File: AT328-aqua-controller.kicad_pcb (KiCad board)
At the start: 2 copper layers, 76.6 x 76 mm, 46 parts, among them Q1 IRL520N, Q2 IRL520N, Q3 IRL520N, Q4 IRL520N, Q5 BC547, U1 ATmega328P-PU, U2 LM7805_TO220, Y1 16MHz

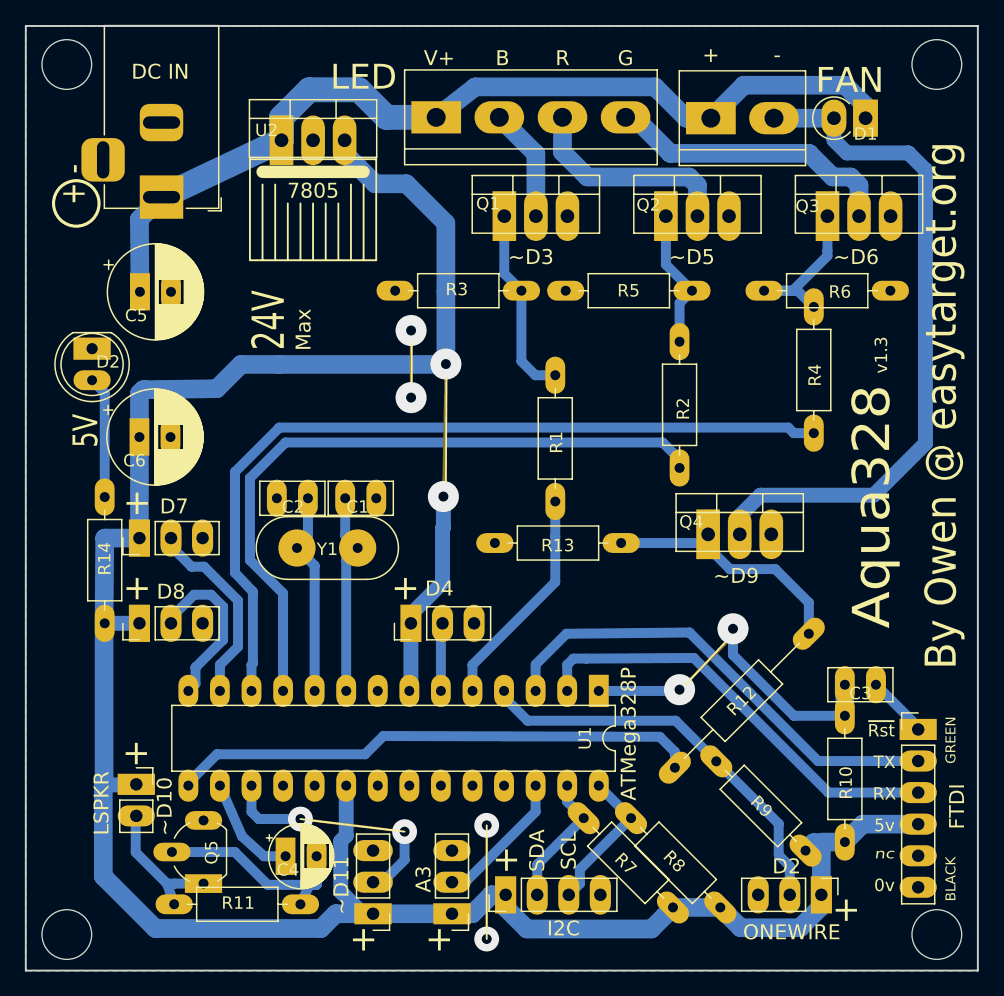
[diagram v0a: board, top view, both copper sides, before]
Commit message: New speaker circuit, updated PCB to suit and slight case mods.
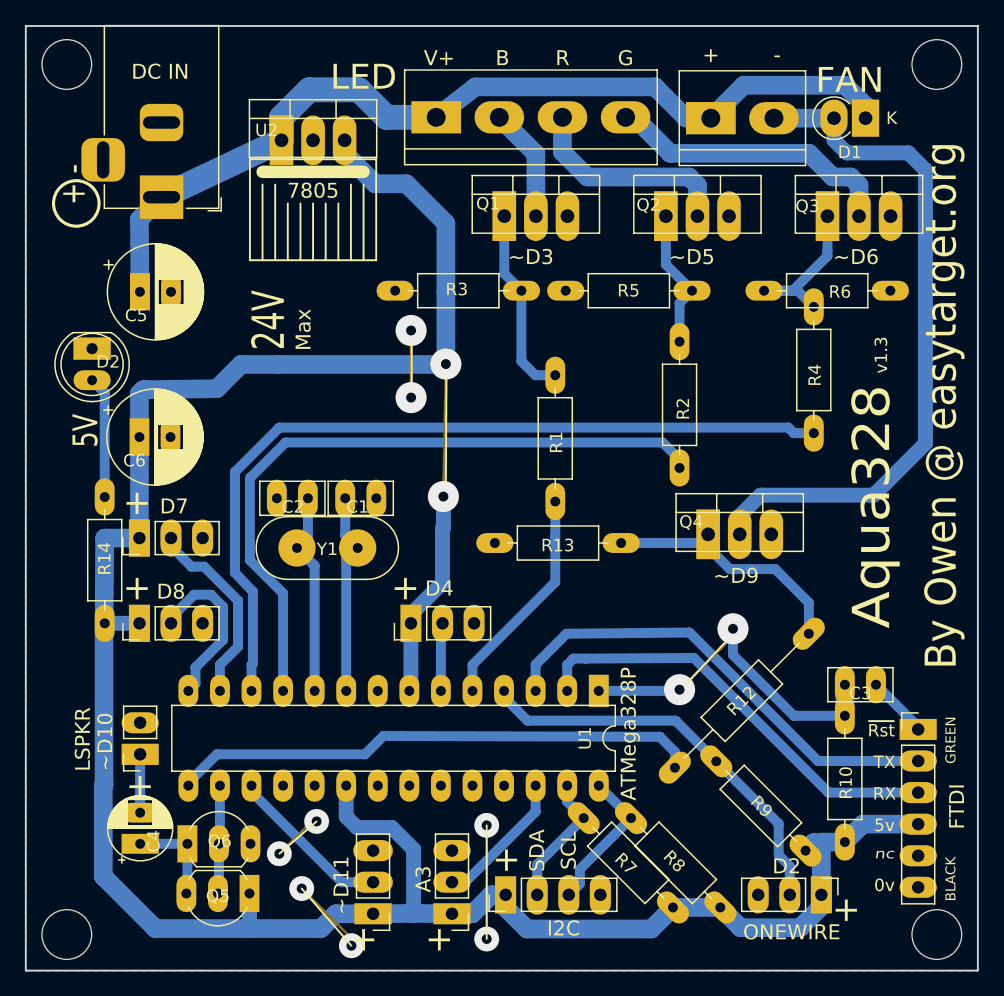
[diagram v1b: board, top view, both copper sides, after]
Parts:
- removed R11: 2K2, Resistor_THT:R_Axial_DIN0207_L6.3mm_D2.5mm_P10.16mm_Horizontal
- added Q6: BC327, Package_TO_SOT_THT:TO-92_Inline_Wide, F.Cu at (44.8, 93.3)
- C4: value 47uF -> 470uF
- Q5: value BC547 -> BC337; footprint Package_TO_SOT_THT:TO-92_Wide -> Package_TO_SOT_THT:TO-92_Inline_Wide
- moved C4 11.7 mm to (41.0, 93.3), turned to 90 degrees
- moved Q5 3.79 mm to (49.8, 97.3), turned to 180 degrees
- moved SPKR1 2.43 mm to (41.0, 86.1), turned to 180 degrees
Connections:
- C4 pad 1: BUZZ -> Net-(C4-Pad1)
- Q5 pad 1: Net-(Q5-Pad1) -> +5V
- Q5 pad 2: Net-(C4-Pad2) -> BUZZ
- Q5 pad 3: GND -> Net-(C4-Pad1)
- SPKR1 pad 1: +5V -> Net-(C4-Pad2)
- SPKR1 pad 2: Net-(Q5-Pad1) -> GND
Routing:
- net Net-(C4-Pad2): track 17.3 -> 4.70 mm
- net Net-(Q5-Pad1): track 11.3 -> 0.00 mm
- net GND: track 14.5 -> 24.9 mm, vias 4 -> 8
- net Net-(C4-Pad1): track 0.00 -> 7.83 mm
- net AUX1: track 20.3 -> 13.3 mm, vias 2 -> 0
- net +5V: track 213.9 -> 217.0 mm
